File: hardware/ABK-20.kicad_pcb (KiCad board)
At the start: 2 copper layers, 90 x 90 mm, 72 parts, among them J1 CONN_01X04, J2 CONN_01X04, J3 CONN_02X03, J4 Con_3-5V, J5 USB_C_6P, J6 Sync_Jumper, SW1 SW_SPST, SW2 SW_Push, SW3 SW_SPDT_MSM, SW4 SW_Push, U1 ATTINY85-20SU, U2 PAM8002, U3 7805

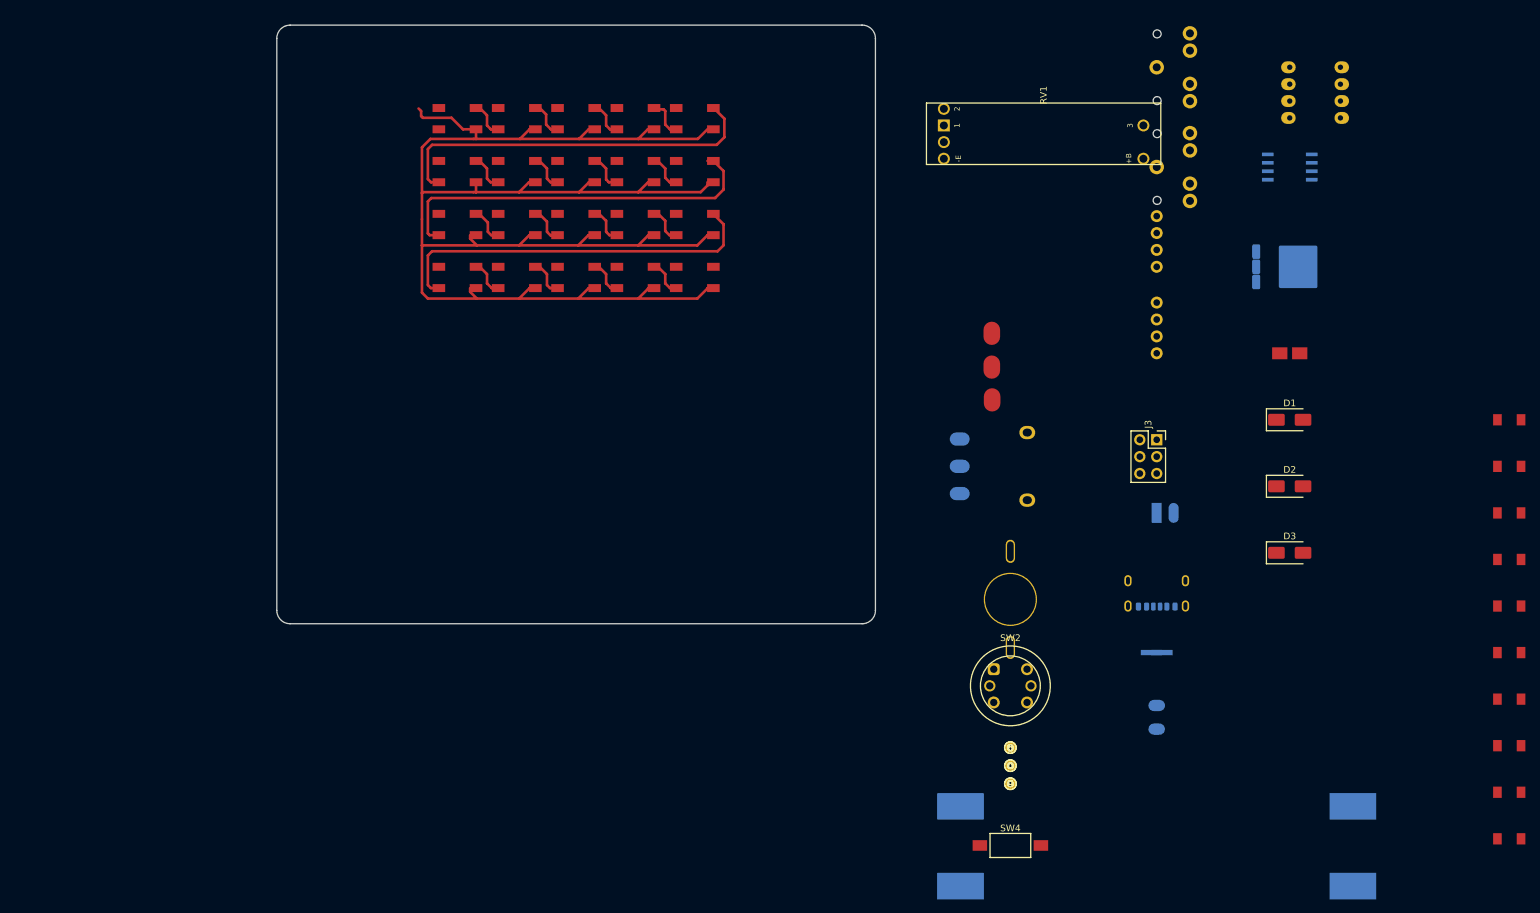
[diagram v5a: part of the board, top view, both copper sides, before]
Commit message: chore(pcb): rearrange components around board for layout placement
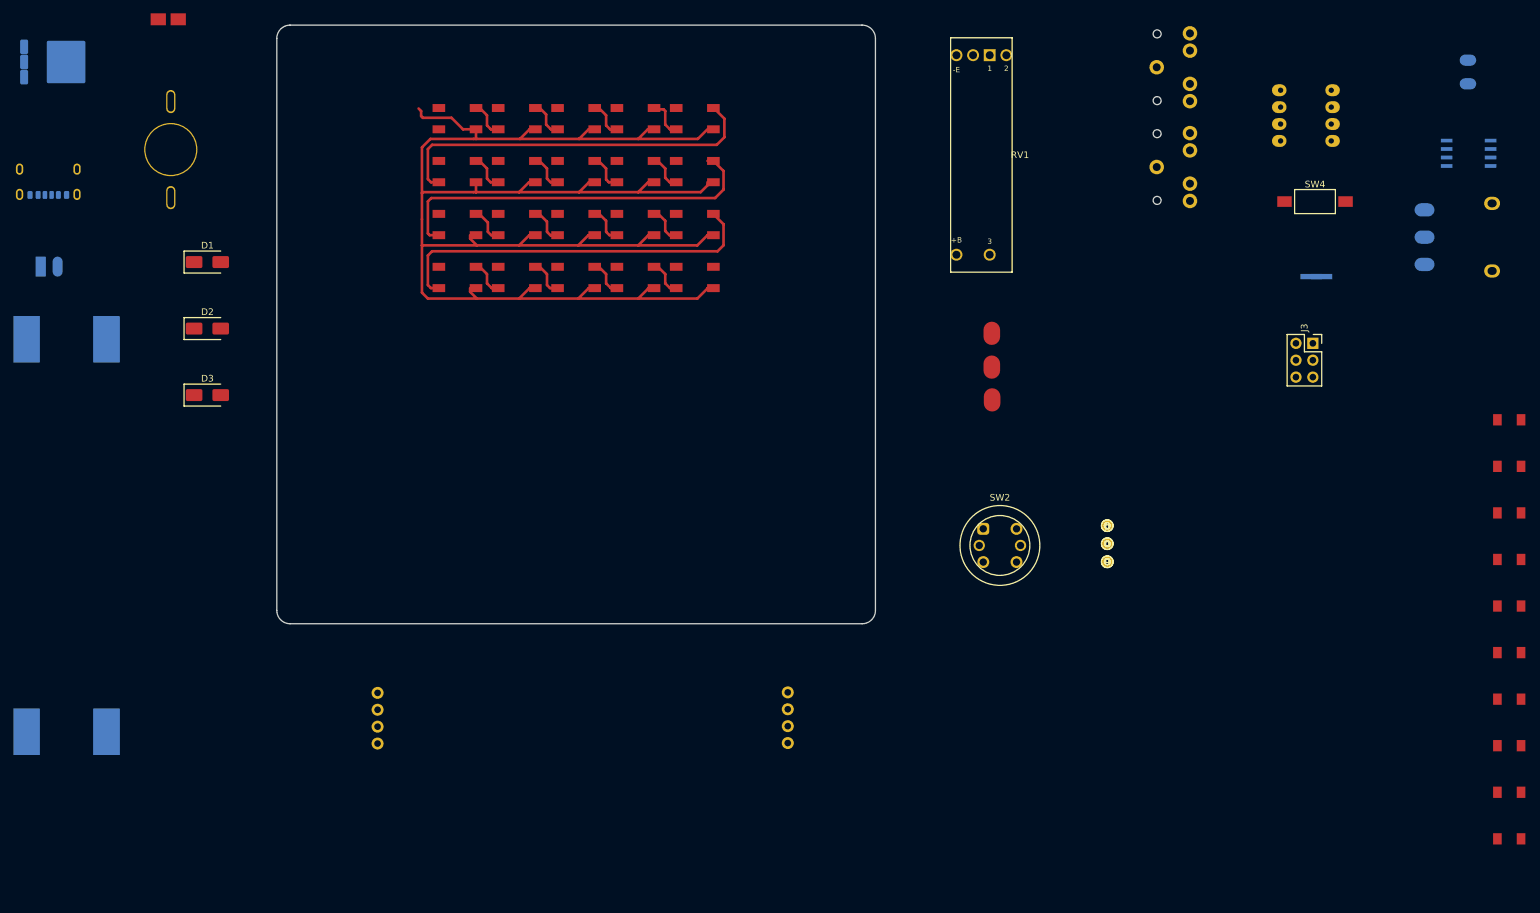
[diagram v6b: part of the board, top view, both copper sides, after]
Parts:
- moved U3 187.8 mm to (36.8, 34.2)
- moved J5 177.8 mm to (35.4, 51.1)
- moved D-POW1 175.9 mm to (53.4, 27.8)
- moved BT1 174.8 mm to (32.0, 105.4), turned to 90 degrees
- moved J4 171.8 mm to (34.2, 65.0)
- moved BT2 166.5 mm to (44.0, 105.4), turned to 90 degrees
- moved D1 164.4 mm to (59.3, 64.3)
- moved D2 164.4 mm to (59.3, 74.3)
- moved D3 164.4 mm to (59.3, 84.3)
- moved SW1 143.2 mm to (53.8, 47.4)
- moved J1 137.3 mm to (84.9, 136.7)
- moved Speaker1 107.7 mm to (248.8, 37.0)
- moved SW4 107.1 mm to (225.8, 55.2)
- moved POT3-Vol1 77.9 mm to (249.9, 60.5)
- moved J2 75.3 mm to (146.5, 129.0), turned to 180 degrees
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
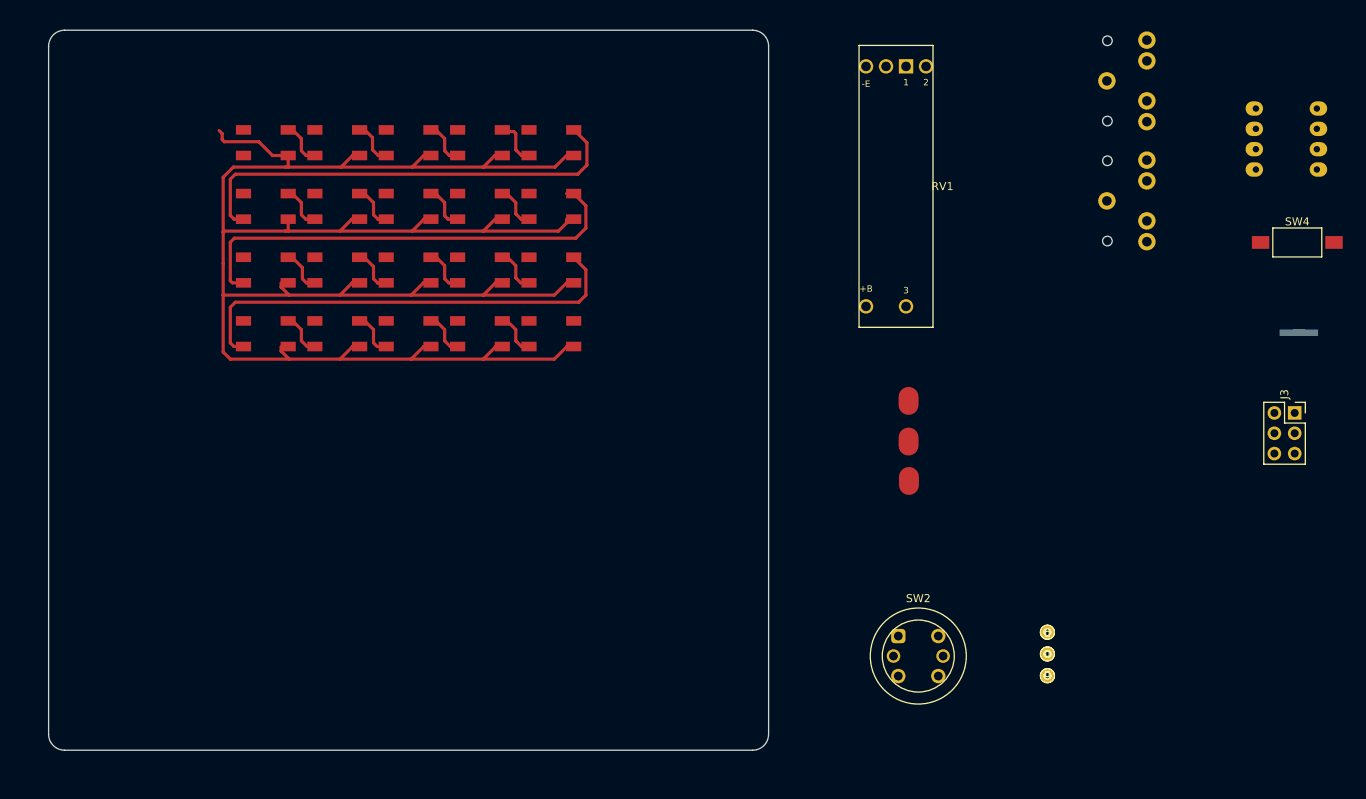
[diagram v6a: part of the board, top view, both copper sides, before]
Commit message: feat(pcb): set board outline to 75x80 mm on Edge.Cuts for compact desktop design
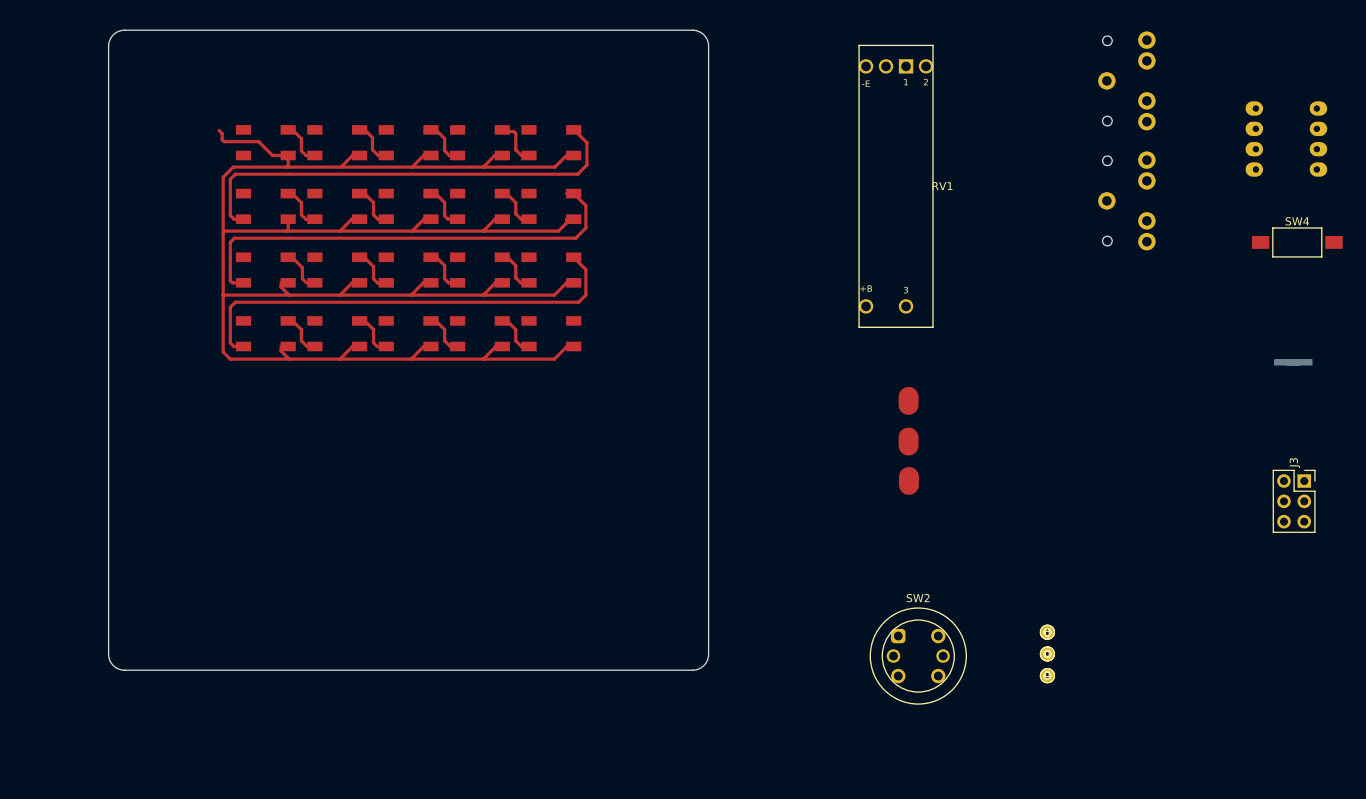
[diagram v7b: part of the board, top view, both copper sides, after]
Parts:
- moved J3 8.59 mm to (226.7, 85.0)
- moved J6 3.77 mm to (225.3, 70.2)
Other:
- board size 90 x 90 mm -> 75 x 80 mm
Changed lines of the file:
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@@
 	(footprint "8Bitmixtape_reworked:Socket_Strip_Straight_2x03_Pitch2.54mm"
 		(layer "F.Cu")
-		(at 225.4758 76.5048)
+		(at 226.6696 85.0138)
 		(descr "Through hole straight socket strip, 2x03, 2.54mm pitch, double rows")
 		(tags "Through hole socket strip THT 2x03 2.54mm double row")
@@
 	(footprint "8Bitmixtape_reworked:Sync_jumper"
 		(layer "B.Cu")
-		(at 225.9964 66.4718)
+		(at 225.298 70.1802)
 		(descr "Resistor SMD 0612, reflow solderinG")
 		(tags "resistor 0612 ")
@@
 	)
 	(gr_arc
-		(start 69.71185 30.66405)
-		(mid 70.297636 29.249836)
-		(end 71.71185 28.66405)
+		(start 77.21185 30.66405)
+		(mid 77.797636 29.249836)
+		(end 79.21185 28.66405)
 		(stroke
 			(width 0.15)
@@
 	)
 	(gr_line
-		(start 69.71185 116.66405)
-		(end 69.71185 30.66405)
+		(start 79.21185 28.66405)
+		(end 150.21185 28.66405)
 		(stroke
 			(width 0.15)
@@
 		(layer "Edge.Cuts")
 	)
-	(gr_line
-		(start 71.71185 28.66405)
-		(end 157.71185 28.66405)
+	(gr_arc
+		(start 150.21185 28.66405)
+		(mid 151.626064 29.249836)
+		(end 152.21185 30.66405)
 		(stroke
 			(width 0.15)
@@
 		(layer "Edge.Cuts")
 	)
-	(gr_arc
-		(start 71.71185 118.66405)
-		(mid 70.297636 118.078264)
-		(end 69.71185 116.66405)
+	(gr_line
+		(start 152.21185 30.66405)
+		(end 152.21185 106.66405)
 		(stroke
 			(width 0.15)
@@
 	)
 	(gr_arc
-		(start 157.71185 28.66405)
-		(mid 159.126064 29.249836)
-		(end 159.71185 30.66405)
+		(start 152.21185 106.66405)
+		(mid 151.626064 108.078264)
+		(end 150.21185 108.66405)
 		(stroke
 			(width 0.15)
@@
 	)
 	(gr_line
-		(start 157.71185 118.66405)
-		(end 71.71185 118.66405)
+		(start 150.21185 108.66405)
+		(end 79.21185 108.66405)
 		(stroke
 			(width 0.15)
@@
 		(layer "Edge.Cuts")
 	)
-	(gr_line
-		(start 159.71185 30.66405)
-		(end 159.71185 116.66405)
+	(gr_arc
+		(start 79.21185 108.66405)
+		(mid 77.797636 108.078264)
+		(end 77.21185 106.66405)
 		(stroke
 			(width 0.15)
@@
 		(layer "Edge.Cuts")
 	)
-	(gr_arc
-		(start 159.71185 116.66405)
-		(mid 159.126064 118.078264)
-		(end 157.71185 118.66405)
+	(gr_line
+		(start 77.21185 106.66405)
+		(end 77.21185 30.66405)
 		(stroke
 			(width 0.15)

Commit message: feat(pcb): finalize 75x80 component placement, self-contained 3D models, and variant showcase
- Place all core components on 75x80 mm board outline: 5x4 NeoPixel matrix, ATtiny85 DIP socket, Bourns slide pot, thumbwheel pot, illuminated RV09 pot, toggle switch, jacks, buttons, and side headers
- Create self-contained local 3D VRML library in hardware/3d_models/ with all project models bundled
- Add ABK-20_showcase_variants.kicad_pcb as standalone comparison showroom
- Fix pin numbering on 7805 voltage regulator (U3) and potentiometer mounting tabs (MP/L)
- Clean up jumper footprints and synchronize schematic assignments
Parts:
- removed BT1, BT2: Battery_Cell, 8Bitmixtape_reworked:BAT_Holder_AAA-new_noHole
- removed J3: CONN_02X03, 8Bitmixtape_reworked:Socket_Strip_Straight_2x03_Pitch2.54mm
- J6: footprint 8Bitmixtape_reworked:Sync_jumper -> 8Bitmixtape_reworked:Sync_jumper_small
- Jack1, Jack2: footprint 8Bitmixtape_reworked:AUDIO-Jack_3.5mm_5Pin -> 8Bitmixtape_reworked:AUDIO-Jack_3.5mm_PJ-317; moved to F.Cu
- POT2-CV1: footprint 8Bitmixtape_reworked:Potentiometer_backPads_noHole -> 8Bitmixtape_reworked:Potentiometer_RV09_Vertical_ClearShaft
- SW2: value SW_Push -> SW_Push_LED
- SW3: footprint 8Bitmixtape_reworked:SWITCH-SPDT_KIT -> 8Bitmixtape_reworked:SW_Toggle_SPDT_MTS-102
- moved C2 203.8 mm to (96.9, 132.5)
- moved C3 203.8 mm to (96.9, 140.5)
- moved C4 203.8 mm to (96.9, 148.5)
- moved C5 203.8 mm to (96.9, 156.5)
- moved C6 203.8 mm to (96.9, 164.5)
- moved C7 203.8 mm to (96.9, 172.5)
- moved C8 203.8 mm to (96.9, 180.5)
- moved C1 203.5 mm to (96.9, 123.7)
- moved R1 154.7 mm to (127.6, 126.8)
- moved R2 154.7 mm to (127.6, 133.8)
- moved R3 154.7 mm to (127.6, 140.8)
- moved R4 154.7 mm to (127.6, 147.8)
- moved R5 154.7 mm to (127.6, 154.8)
- moved R6 154.7 mm to (127.6, 161.8)
- moved R7 154.7 mm to (127.6, 168.8)
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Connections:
- SW2 pad A: (no net) -> unconnected-(SW2-PadA)
- SW2 pad K: (no net) -> unconnected-(SW2-PadK)
- U3 pad 1: (no net) -> DC_in
- U3 pad 2: (no net) -> GND
- U3 pad 3: (no net) -> Net-(D1-A)
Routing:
- net VCC: track 239.5 -> 237.8 mm
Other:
- board size 75 x 80 mm -> 175 x 80 mm
